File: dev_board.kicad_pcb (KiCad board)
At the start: 2 copper layers, 64 x 24 mm, 43 parts, among them J1 USB_C_Receptacle_USB2.0_16P, J2 Conn_01x20_Pin, J3 Conn_01x20_Pin, J4 Conn_01x04_Pin, SW1 SW_SPST, SW2 SW_SPST, U1 STM32F103C8Tx, U2 AMS1117-3.3, U3 USBLC6-2SC6, Y1 16MHz

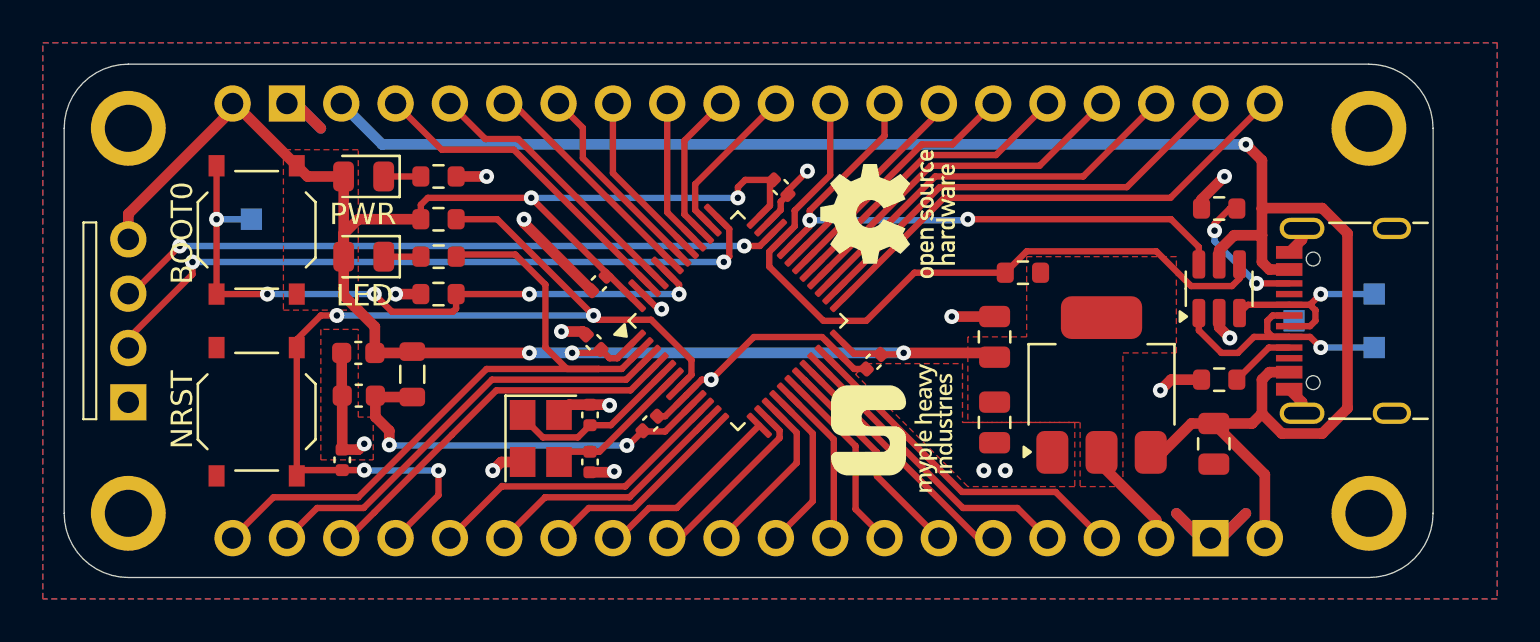
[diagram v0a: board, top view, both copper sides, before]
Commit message: opt: zone fills and remove some vias after feedback
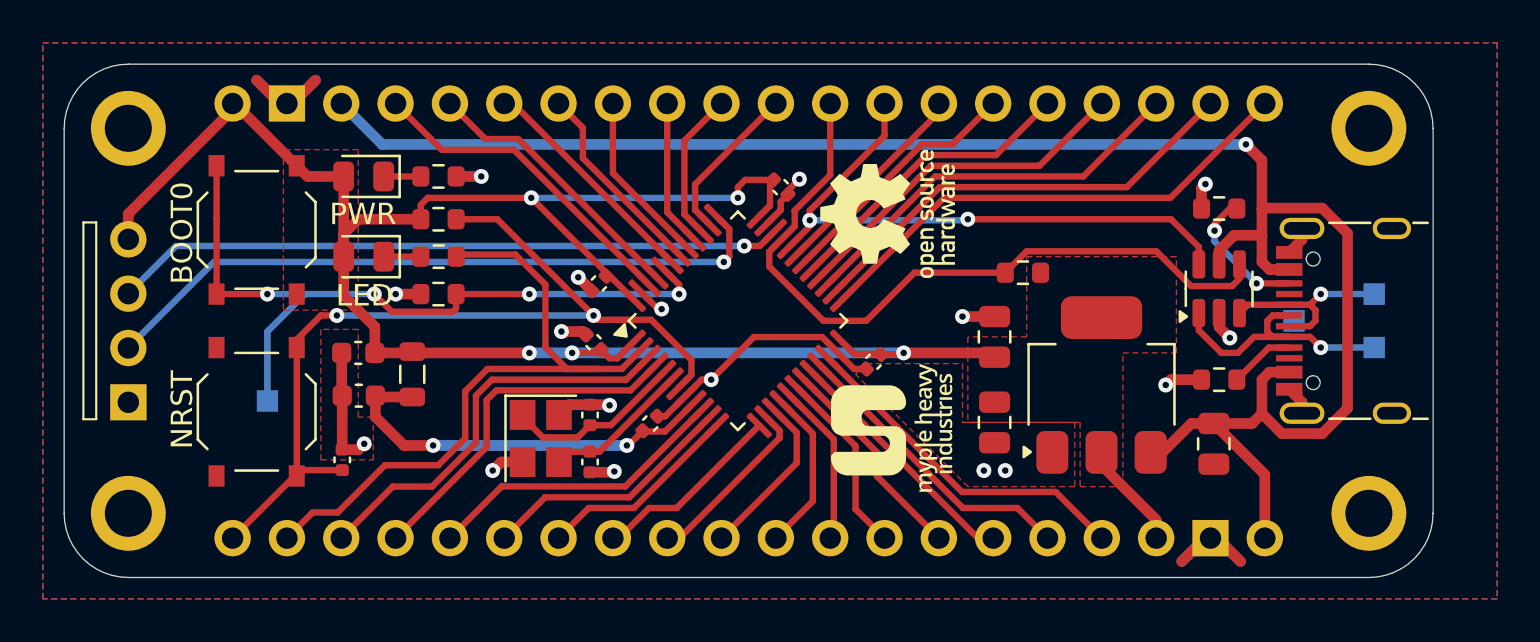
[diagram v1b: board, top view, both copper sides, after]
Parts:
- moved TP4 8.53 mm to (120.5, 106.8)
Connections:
- J3 pad 17: /NRST -> /C15
- J3 pad 18: /C15 -> /C14
- J3 pad 19: /C14 -> /C13
- J3 pad 20: /C13 -> /NRST
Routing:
- net /NRST: track 46.7 -> 42.4 mm, vias 4 -> 2
- net /BOOT0: track 31.8 -> 35.9 mm, vias 5 -> 4
- net GND: track 57.7 -> 54.6 mm
- net /C15: track 18.1 -> 16.8 mm
- net /C13: track 33.4 -> 32.1 mm
- net /C14: track 20.4 -> 19.5 mm
- net /SWCLK: track 32.6 -> 32.0 mm, vias 2 -> 1
- net /SWDIO: vias 2 -> 1

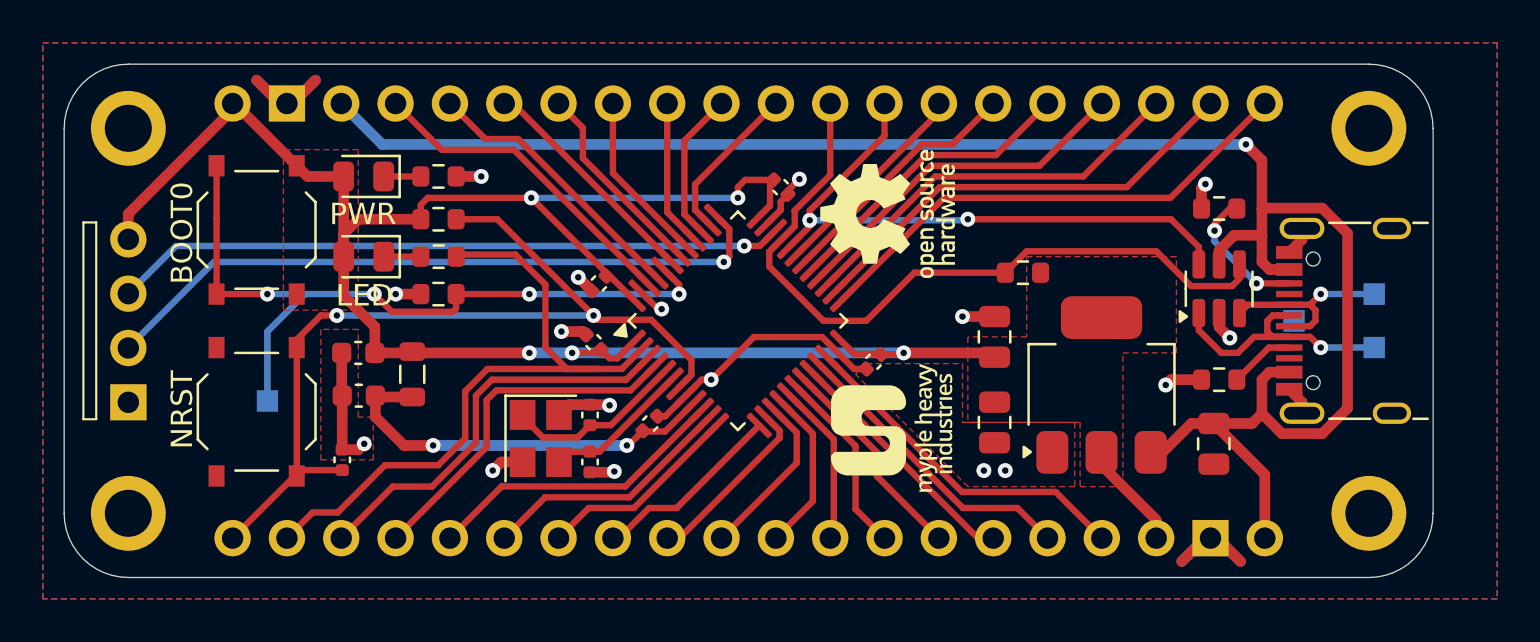
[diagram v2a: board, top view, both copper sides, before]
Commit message: feat: round tracks
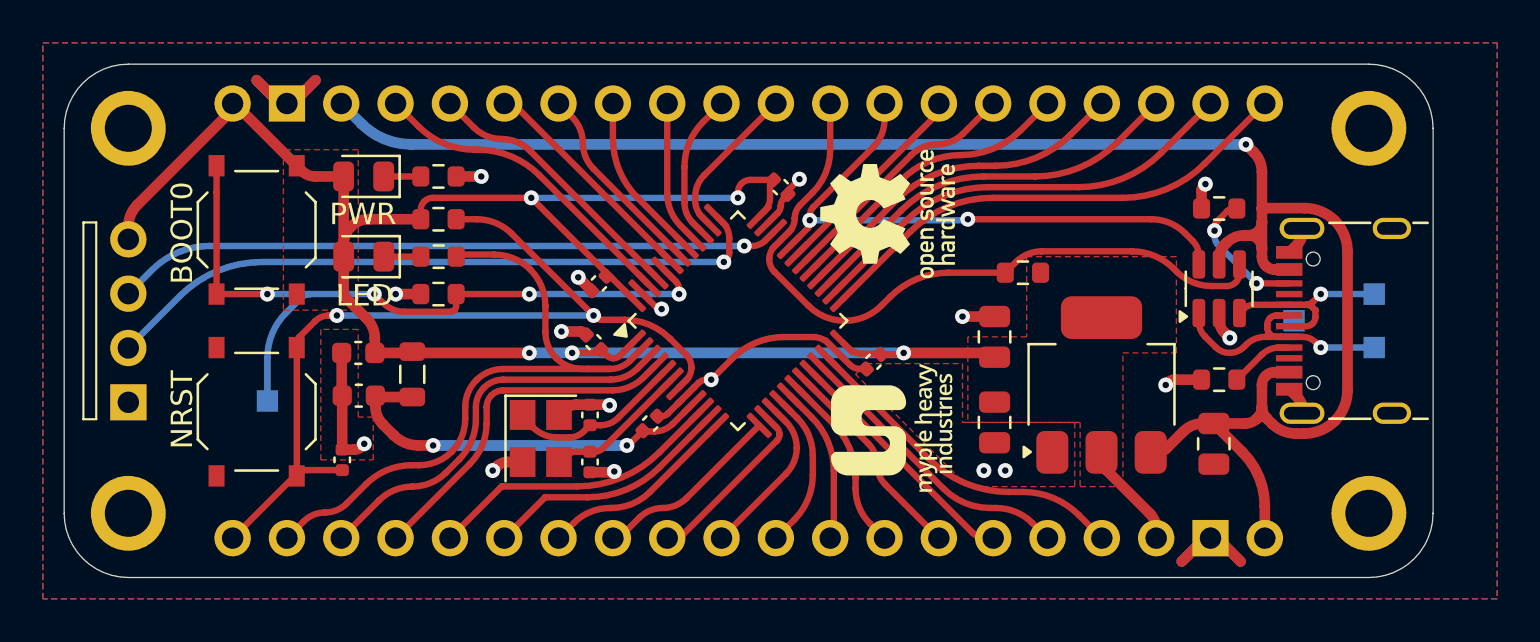
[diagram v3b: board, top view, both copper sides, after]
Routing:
- net /A12: track 34.7 -> 33.6 mm
- net +3.3V: track 96.4 -> 95.3 mm
- net VBUS: track 86.1 -> 87.0 mm
- net /C14: track 19.5 -> 18.8 mm
- net GND: track 54.6 -> 53.9 mm
- net /C13: track 32.1 -> 31.5 mm
- net /B12: track 23.5 -> 23.0 mm
- net /B13: track 21.2 -> 20.7 mm
- net /B14: track 18.9 -> 18.4 mm
- net /B15: track 16.5 -> 16.0 mm
